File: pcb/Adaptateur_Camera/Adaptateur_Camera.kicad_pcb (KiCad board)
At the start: 2 copper layers, 76 x 50 mm, 8 parts, among them CN1 FTR-105-03-G-D-P-TR, P1 TE-FFC-8-0.5

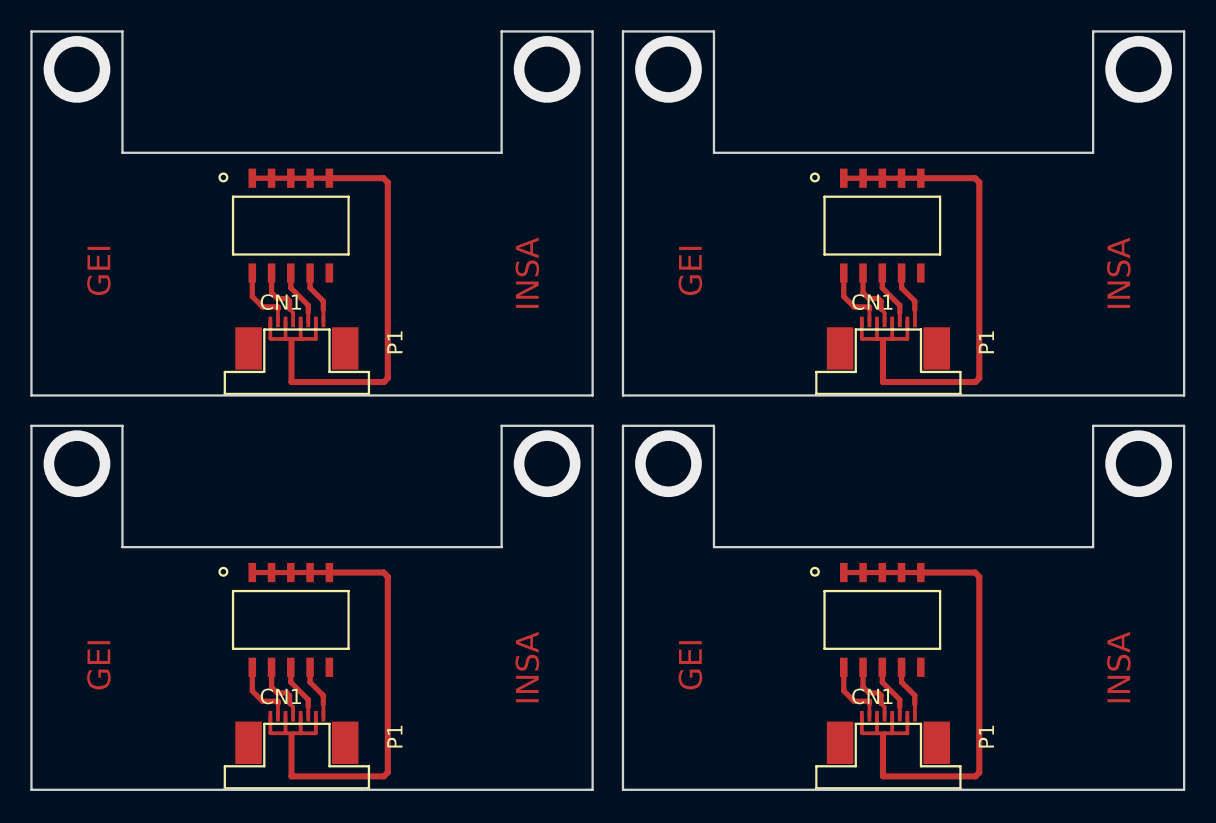
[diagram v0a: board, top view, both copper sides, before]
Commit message: Correction sur l'adaptateur Camera / Ajout du pcb de l'encodeur optique
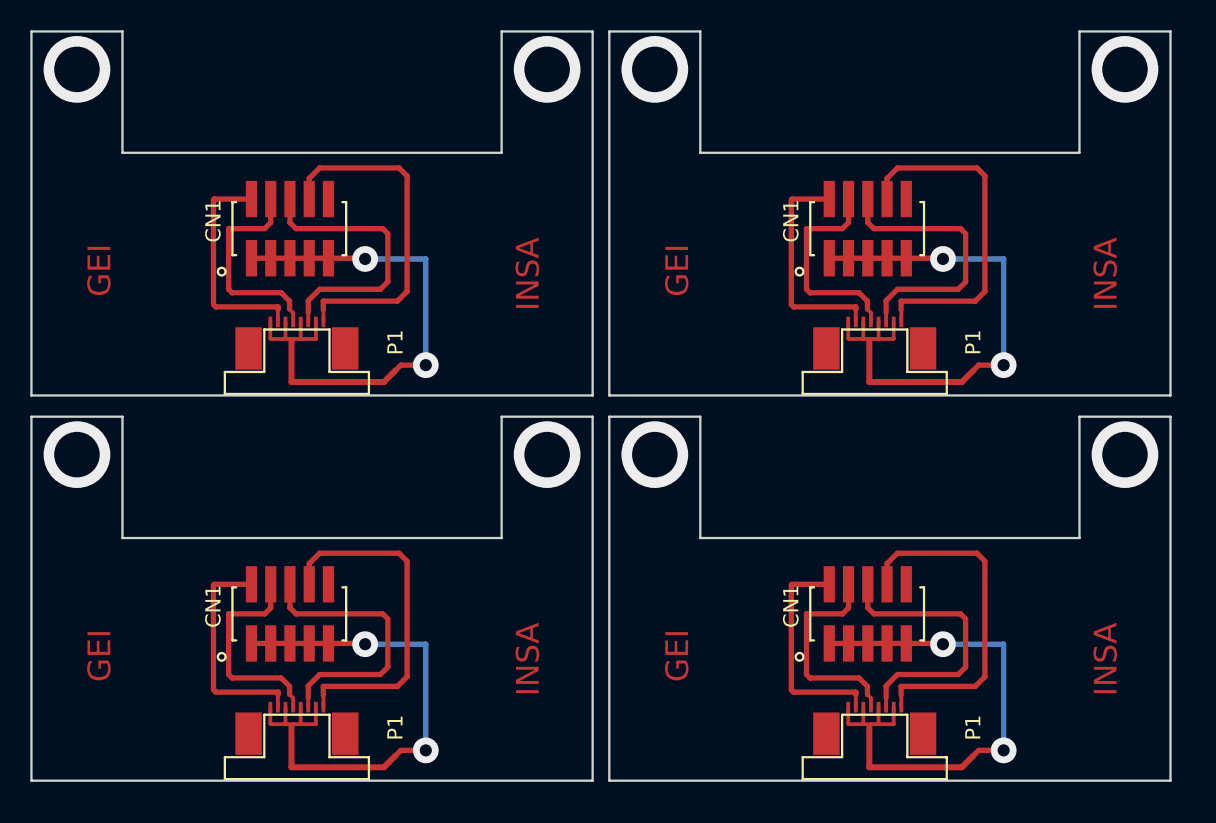
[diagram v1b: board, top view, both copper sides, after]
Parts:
- removed the CN1 at (136.1, 128.8)
- removed the CN1 at (97.1, 128.8)
- removed the CN1 at (136.1, 102.8)
- removed the CN1 at (97.1, 102.8)
- removed the P1 at (136.5, 135.5)
- removed the P1 at (97.5, 135.5)
- removed the P1 at (136.5, 109.5)
- added CN1: FTR-105-03-G-D-P-TR, Insa:FTSH-10-1.27, F.Cu at (135.1, 128.4)
- added CN1: FTR-105-03-G-D-P-TR, Insa:FTSH-10-1.27, F.Cu at (97.0, 128.4)
- added CN1: FTR-105-03-G-D-P-TR, Insa:FTSH-10-1.27, F.Cu at (135.1, 103.0)
- added CN1: FTR-105-03-G-D-P-TR, Insa:FTSH-10-1.27, F.Cu at (97.0, 103.0)
- added P1: TE-FFC-8-0.5, Insa:FFC-8-0.5, F.Cu at (135.6, 134.9)
- added P1: TE-FFC-8-0.5, Insa:FFC-8-0.5, F.Cu at (97.5, 134.9)
- added P1: TE-FFC-8-0.5, Insa:FFC-8-0.5, F.Cu at (135.6, 109.5)
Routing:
- net (no net): track 163.8 -> 326.4 mm, vias 8 -> 14
- net VDD: track 3.59 -> 23.1 mm
- net /CCD_CLK: track 3.70 -> 18.6 mm
- net /CCD_AD: track 4.53 -> 14.7 mm
- net /CCD_SI: track 4.19 -> 14.3 mm
- net GND: track 38.6 -> 38.0 mm, vias 0 -> 2
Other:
- board size 76 x 50 mm -> 75.1 x 49.4 mm

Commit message: Encoder OK, Camera OK
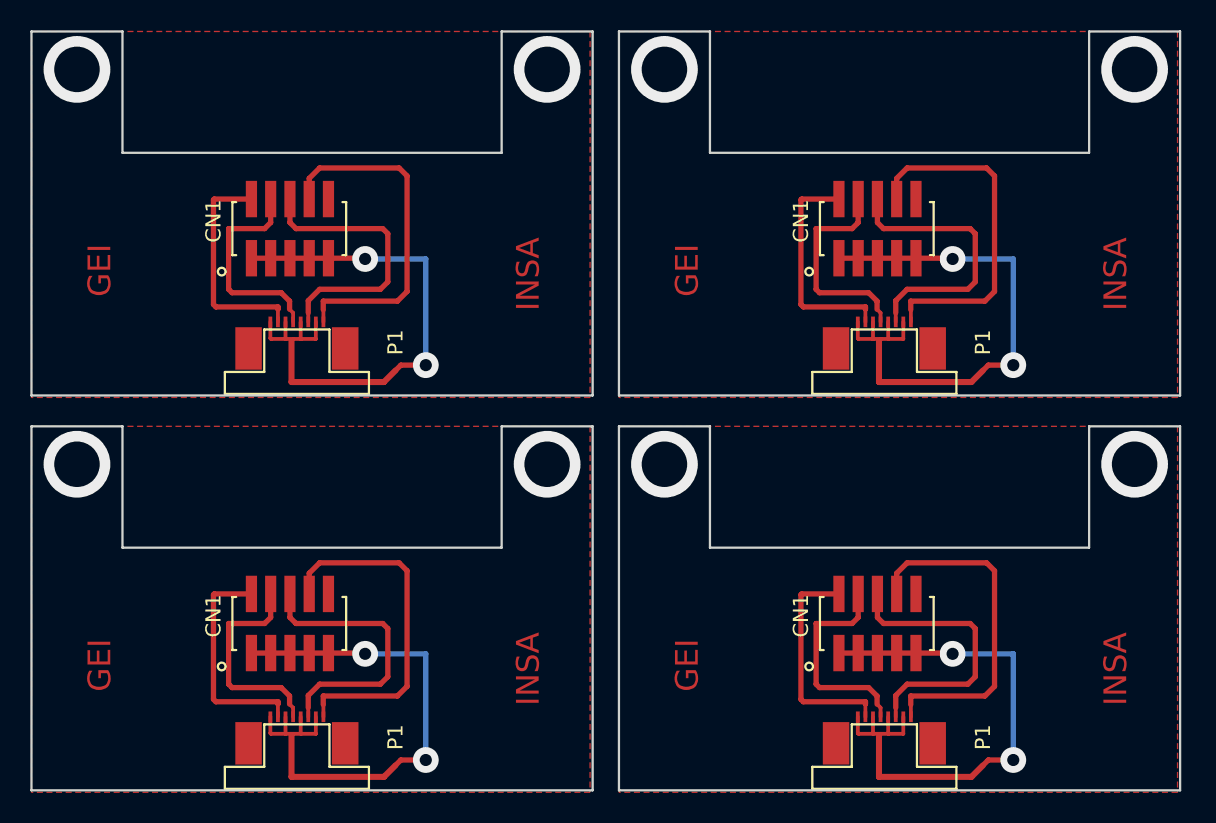
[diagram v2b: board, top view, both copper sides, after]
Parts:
- removed the CN1 at (135.1, 128.4)
- removed the CN1 at (97.0, 128.4)
- removed the CN1 at (135.1, 103.0)
- removed the P1 at (135.6, 134.9)
- removed the P1 at (97.5, 134.9)
- removed the P1 at (135.6, 109.5)
- added CN1: FTR-105-03-G-D-P-TR, Insa:FTSH-10-1.27, F.Cu at (97.0, 129.0)
- added CN1: FTR-105-03-G-D-P-TR, Insa:FTSH-10-1.27, F.Cu at (135.7, 129.0)
- added CN1: FTR-105-03-G-D-P-TR, Insa:FTSH-10-1.27, F.Cu at (135.7, 103.0)
- added P1: TE-FFC-8-0.5, Insa:FFC-8-0.5, F.Cu at (136.2, 135.5)
- added P1: TE-FFC-8-0.5, Insa:FFC-8-0.5, F.Cu at (97.5, 135.5)
- added P1: TE-FFC-8-0.5, Insa:FFC-8-0.5, F.Cu at (136.2, 109.5)
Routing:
- added copper zone on F.Cu, net (none)
- added copper zone on F.Cu, net GND
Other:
- board size 75.1 x 49.4 mm -> 75.7 x 50 mm
